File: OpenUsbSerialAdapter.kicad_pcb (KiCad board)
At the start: 2 copper layers, 17 parts, among them J1 USB_A, J2 FTDI, U1 MCP2200-I-SO, Y1 12M

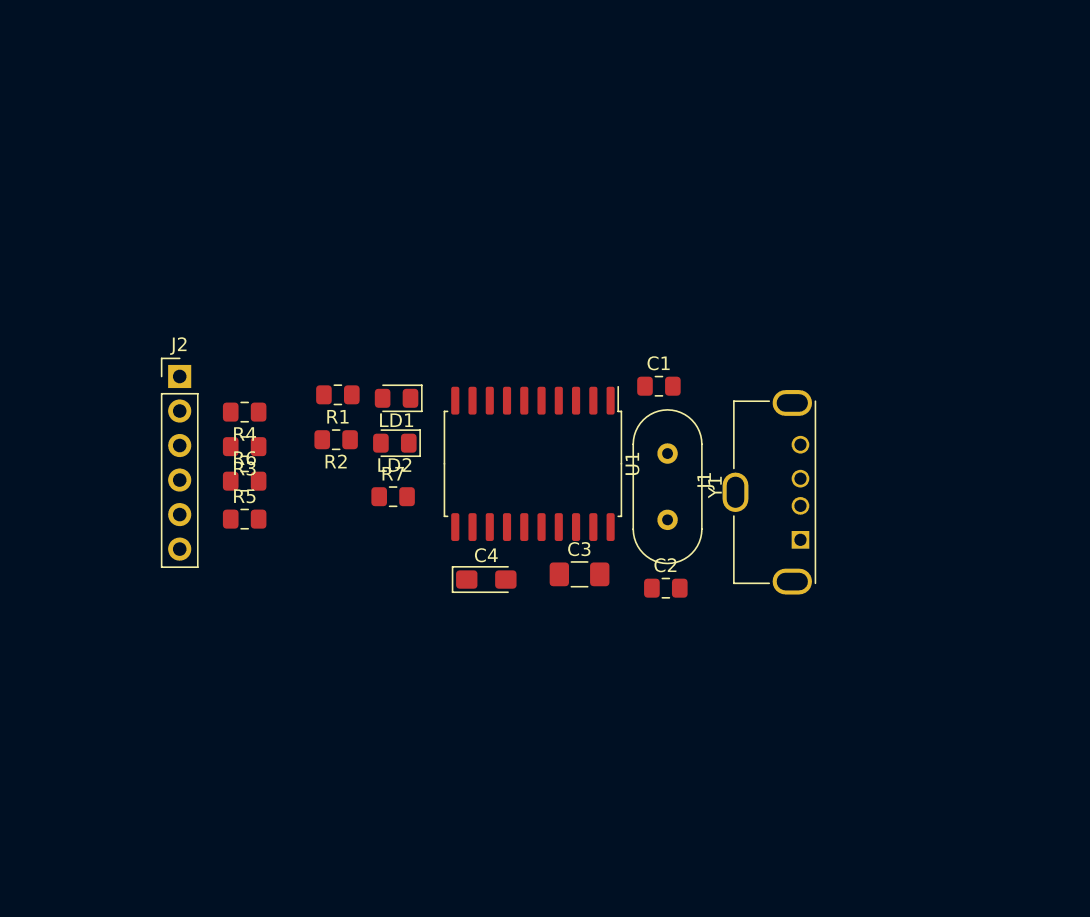
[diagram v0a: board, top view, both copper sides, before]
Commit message: PCB is routed
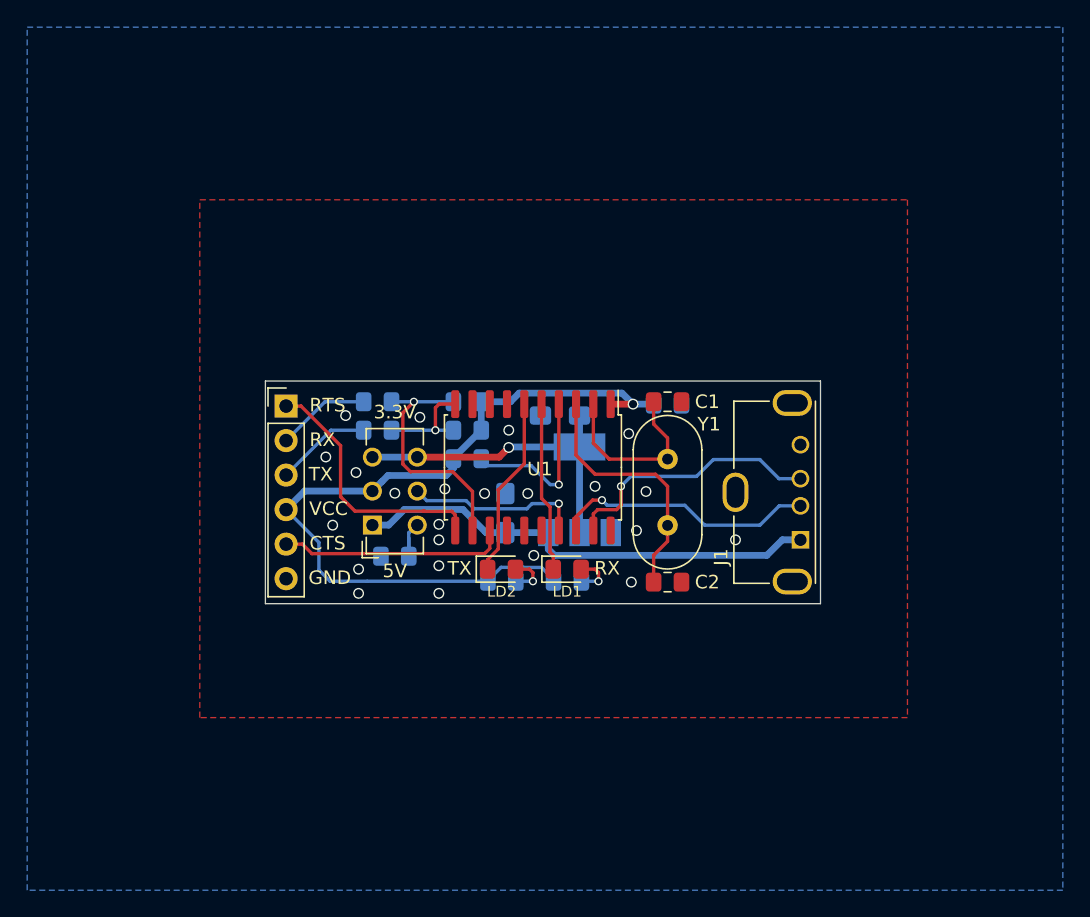
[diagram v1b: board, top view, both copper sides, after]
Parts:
- added C5: 10u, Capacitor_Tantalum_SMD:CP_EIA-3216-18_Kemet-A_Pad1.58x1.35mm_HandSolder, B.Cu at (149.5, 99.2)
- added C6: 10u, Capacitor_Tantalum_SMD:CP_EIA-3216-18_Kemet-A_Pad1.58x1.35mm_HandSolder, B.Cu at (153.5, 92.1)
- added SW1: SW_DPDT_x2, Button_Switch_THT:SW_CuK_JS202011CQN_DPDT_Straight, F.Cu at (139.7, 100.1)
- added U2: AMS1117-3.3, Package_TO_SOT_SMD:SOT-223-3_TabPin2, B.Cu at (154.9, 97.5)
- C3: value 220u -> 330n; footprint Capacitor_SMD:C_1206_3216Metric_Pad1.42x1.75mm_HandSolder -> Capacitor_SMD:C_0805_2012Metric_Pad1.15x1.40mm_HandSolder; moved to B.Cu
- C4: value CP1 -> 100n; footprint Capacitor_Tantalum_SMD:CP_EIA-3216-18_Kemet-A_Pad1.58x1.35mm_HandSolder -> Capacitor_SMD:C_0805_2012Metric_Pad1.15x1.40mm_HandSolder; moved to B.Cu
- R1, R2, R3, R4, R5, R6, R7: moved to B.Cu
- moved R1 21.8 mm to (154.1, 104.3)
- moved C4 18.6 mm to (161.4, 91.2)
- moved R5 18.5 mm to (146.7, 91.1), turned to 180 degrees
- moved LD1 17.8 mm to (154.0, 103.4), turned to 0 degrees
- moved R6 16.8 mm to (146.7, 93.2), turned to 180 degrees
- moved R2 16.0 mm to (149.2, 104.3)
- moved C3 13.7 mm to (141.3, 102.4), turned to 180 degrees
- moved LD2 12.1 mm to (149.2, 103.4), turned to 0 degrees
- moved R3 9.85 mm to (140.1, 93.2)
- moved R4 9.81 mm to (140.1, 91.1)
- moved J2 8.12 mm to (133.3, 91.4)
- moved R7 6.13 mm to (146.7, 95.2)
- moved C1 1.31 mm to (161.4, 91.1), turned to 180 degrees
- moved C2 0.46 mm to (161.4, 104.3), turned to 180 degrees
- moved Y1 0.41 mm to (161.4, 95.3)
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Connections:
- C4 pad 1: +5V -> VCC
- J2 pad 4: +5V -> VCC
- R1 pad 2: +5V -> VCC
- R2 pad 2: +5V -> VCC
- R5 pad 1: +5V -> VCC
- R6 pad 1: +5V -> VCC
- R7 pad 1: +5V -> VCC
- U1 pad 1: +5V -> VCC
- U1 pad 17: Net-(C3-Pad1) -> Net-(SW1-Pad5)
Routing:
- net VCC: track 0.00 -> 58.2 mm, vias 0 -> 1
- net +5V: track 0.00 -> 34.6 mm
- net +3V3: track 0.00 -> 24.3 mm, vias 0 -> 1
- net /usb+: track 0.00 -> 19.5 mm, vias 0 -> 1
- net Net-(C2-Pad2): track 0.00 -> 19.5 mm
- net /usb-: track 0.00 -> 19.4 mm, vias 0 -> 1
- net /~rts: track 0.00 -> 19.1 mm
- net Net-(R4-Pad1): track 0.00 -> 18.5 mm, vias 0 -> 1
- net /~cts: track 0.00 -> 17.0 mm
- net Net-(C1-Pad2): track 0.00 -> 14.0 mm
- net Net-(LD2-Pad1): track 0.00 -> 13.3 mm
- net Net-(SW1-Pad5): track 0.00 -> 13.1 mm, vias 0 -> 1
- net Net-(LD1-Pad1): track 0.00 -> 12.5 mm
- net Net-(R7-Pad2): track 0.00 -> 12.4 mm, vias 0 -> 1
- net Net-(R3-Pad1): track 0.00 -> 7.78 mm, vias 0 -> 1
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- added copper zone on B.Cu, net GND
- added copper zone on F.Cu, net GND
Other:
- board outline added: 40.8 x 16.4 mm
- net class Default: via_dia 0.8 -> 0.6
- net class Power added: clearance 0.2, trace_width 0.5, via_dia 0.8, via_drill 0.6
- rule pad_to_mask_clearance: 0.051 -> 0
- board text added: "3.3V"
- board text added: "5V"
- board text added: "CTS"
- board text added: "GND"
- board text added: "Licensed under CERN OHL v.1.2"
- board text added: "RTS"
- board text added: "RX"
- board text added: "TX"
- board text added: "VCC"
- board text added: "github.com/SukkoPera/ OpenUsbSerialAdapter"

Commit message: Done! (Again...)
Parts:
- C3: footprint Capacitor_SMD:C_0805_2012Metric_Pad1.15x1.40mm_HandSolder -> Capacitor_SMD:C_1206_3216Metric_Pad1.42x1.75mm_HandSolder
- J1: footprint Connector_USB:USB_A_Molex_105057_Vertical -> OpenUsbSerialAdapter:USB_A_Molex_48037
- moved J1 4.25 mm to (168.8, 97.7)
- moved C3 0.06 mm to (141.4, 102.5)
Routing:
- net /usb-: track 19.4 -> 13.7 mm
- net /usb+: track 19.5 -> 13.8 mm
- net +5V: track 34.6 -> 29.8 mm
- net Net-(C3-Pad1): track 3.84 -> 2.65 mm
- net GND: vias 23 -> 22
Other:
- board size 40.8 x 16.4 mm -> 39.8 x 16.4 mm
- board text added: "V1"

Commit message: Some refinements
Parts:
- J2: footprint Connector_PinHeader_2.54mm:PinHeader_1x06_P2.54mm_Vertical -> OpenUsbSerialAdapter:PinHeader_1x06_P2.54mm_Vertical
- moved R3 0.38 mm to (139.7, 93.2)
- moved R4 0.38 mm to (139.7, 91.1)
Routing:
- net Net-(R4-Pad1): track 18.5 -> 19.1 mm

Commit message: Final touches
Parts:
- SW1: footprint Button_Switch_THT:SW_CuK_JS202011CQN_DPDT_Straight -> OpenUsbSerialAdapter:SW_DPDT
